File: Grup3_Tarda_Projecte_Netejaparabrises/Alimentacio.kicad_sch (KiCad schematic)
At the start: 14 parts, among them IC1 L78S05CV, J1 Screw_Terminal_01x02

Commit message: canvis reles
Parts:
- FL1, FL2, FL3, FL4: footprint BLM03HD331SZ1D:BEADC0603X33N -> Projecte:BEADC0603X33N
- IC1: footprint L78S05CV:TO-220-STANDING -> Projecte:TO-220-STANDING
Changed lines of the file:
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@@
       (effects (font (size 1.27 1.27)))
     )
-    (property "Footprint" "BLM03HD331SZ1D:BEADC0603X33N" (at 95.25 134.62 0)
+    (property "Footprint" "Projecte:BEADC0603X33N" (at 95.25 134.62 0)
       (effects (font (size 1.27 1.27)) (justify bottom) hide)
     )
@@
       (effects (font (size 1.27 1.27)))
     )
-    (property "Footprint" "BLM03HD331SZ1D:BEADC0603X33N" (at 95.25 143.51 0)
+    (property "Footprint" "Projecte:BEADC0603X33N" (at 95.25 143.51 0)
       (effects (font (size 1.27 1.27)) (justify bottom) hide)
     )
@@
       (effects (font (size 1.27 1.27)))
     )
-    (property "Footprint" "BLM03HD331SZ1D:BEADC0603X33N" (at 95.25 115.57 0)
+    (property "Footprint" "Projecte:BEADC0603X33N" (at 95.25 115.57 0)
       (effects (font (size 1.27 1.27)) (justify bottom) hide)
     )
@@
       (effects (font (size 1.27 1.27)))
     )
-    (property "Footprint" "L78S05CV:TO-220-STANDING" (at 147.574 62.992 0)
+    (property "Footprint" "Projecte:TO-220-STANDING" (at 147.574 62.992 0)
       (effects (font (size 1.27 1.27)) (justify bottom) hide)
     )
@@
       (effects (font (size 1.27 1.27)))
     )
-    (property "Footprint" "BLM03HD331SZ1D:BEADC0603X33N" (at 95.25 124.46 0)
-      (effects (font (size 1.27 1.27)) (justify bottom) hide)
-    )
+    (property "Footprint" "Projecte:BEADC0603X33N" (at 95.25 124.46 0)
+      (effects (font (size 1.27 1.27)) (justify bottom) hide)
+    )

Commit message: Layout 3
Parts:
- FL1, FL2, FL3, FL4: footprint Projecte:BEADC0603X33N -> BLM03HD331SZ1D:BEADC0603X33N
- IC1: footprint Projecte:TO-220-STANDING -> L78S05CV:TO-220-STANDING
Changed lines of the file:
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@@
   (title_block
     (title "Projecte Netejaparabrises - Grup 4 Tarda")
-    (date "2023-04-12")
-    (rev "v1.2.12042023")
+    (date "2023-04-05")
+    (rev "v1.1.05042023")
   )
   (junction (at 132.334 62.992) (diameter 0) (color 0 0 0 0)
@@
       (effects (font (size 1.27 1.27)))
     )
-    (property "Footprint" "Projecte:BEADC0603X33N" (at 95.25 134.62 0)
+    (property "Footprint" "BLM03HD331SZ1D:BEADC0603X33N" (at 95.25 134.62 0)
       (effects (font (size 1.27 1.27)) (justify bottom) hide)
     )
@@
       (effects (font (size 1.27 1.27)))
     )
-    (property "Footprint" "Projecte:BEADC0603X33N" (at 95.25 143.51 0)
+    (property "Footprint" "BLM03HD331SZ1D:BEADC0603X33N" (at 95.25 143.51 0)
       (effects (font (size 1.27 1.27)) (justify bottom) hide)
     )
@@
       (effects (font (size 1.27 1.27)))
     )
-    (property "Footprint" "Projecte:BEADC0603X33N" (at 95.25 115.57 0)
+    (property "Footprint" "BLM03HD331SZ1D:BEADC0603X33N" (at 95.25 115.57 0)
       (effects (font (size 1.27 1.27)) (justify bottom) hide)
     )
@@
       (effects (font (size 1.27 1.27)))
     )
-    (property "Footprint" "Projecte:TO-220-STANDING" (at 147.574 62.992 0)
+    (property "Footprint" "L78S05CV:TO-220-STANDING" (at 147.574 62.992 0)
       (effects (font (size 1.27 1.27)) (justify bottom) hide)
     )
@@
       (effects (font (size 1.27 1.27)))
     )
-    (property "Footprint" "Projecte:BEADC0603X33N" (at 95.25 124.46 0)
-      (effects (font (size 1.27 1.27)) (justify bottom) hide)
-    )
+    (property "Footprint" "BLM03HD331SZ1D:BEADC0603X33N" (at 95.25 124.46 0)
+      (effects (font (size 1.27 1.27)) (justify bottom) hide)
+    )

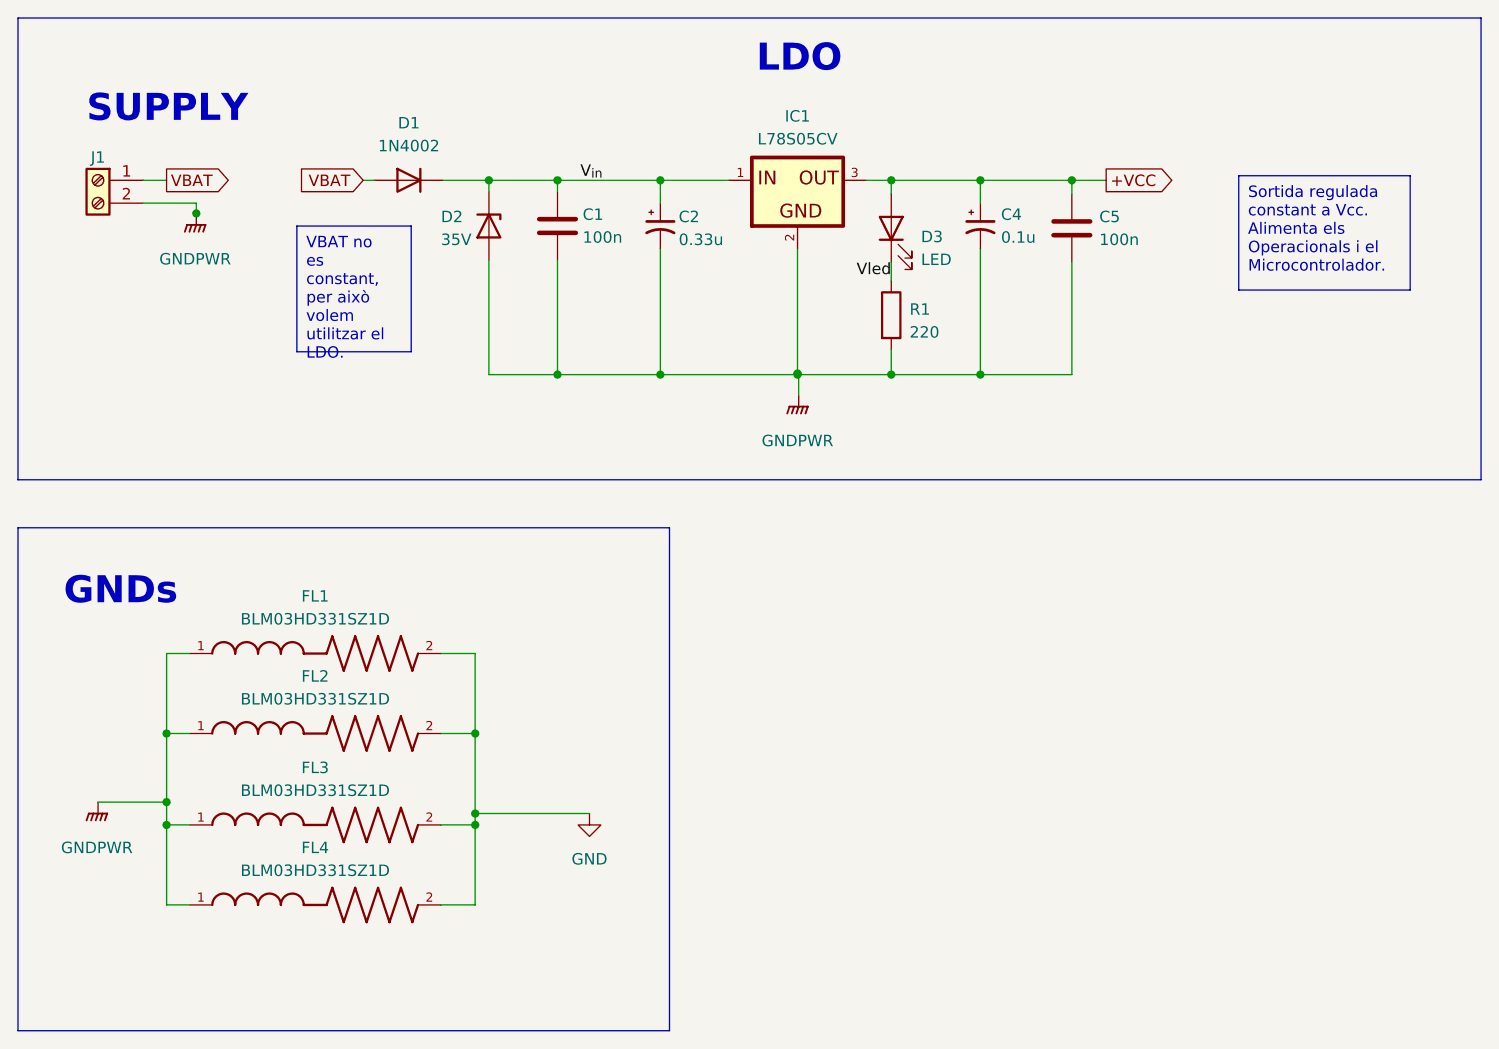
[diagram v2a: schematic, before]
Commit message: canvis divisor sensor de pluja, node vbat protegit, connector de motors, README
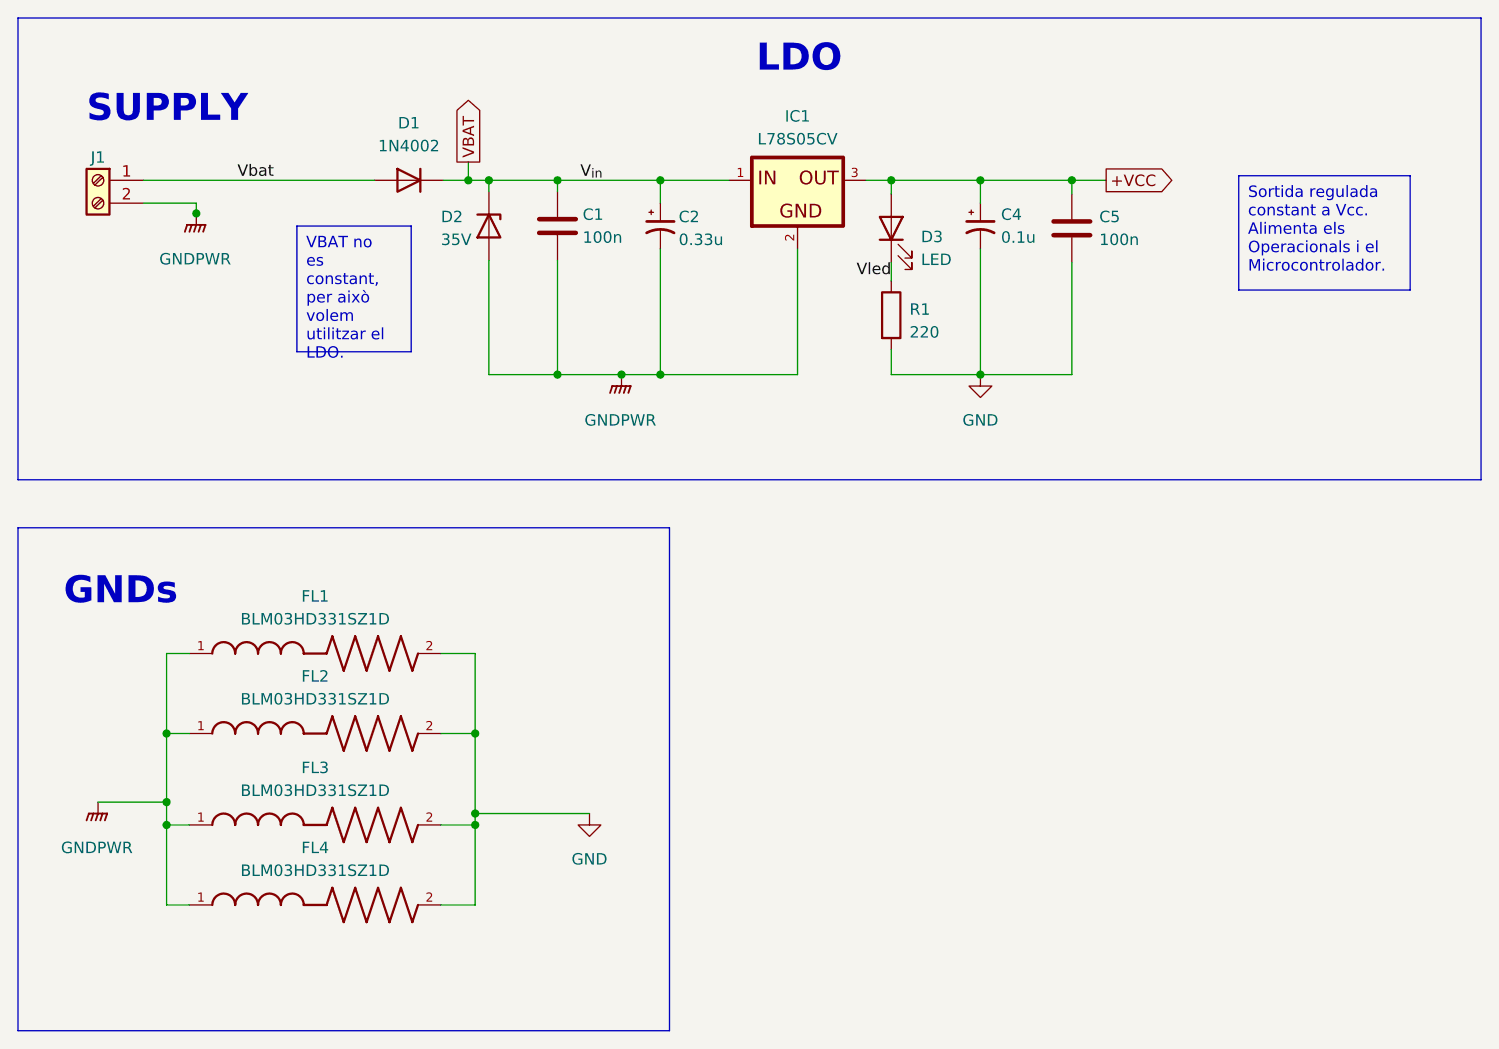
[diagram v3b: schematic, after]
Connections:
- net V_{in} is gone; now on net VBAT: C1.1, C2.1, D1.1 (K), D2.1 (K), IC1.1
- net GND: now also C4.2, C5.2, R1.2
- net GNDPWR: no longer C4.2, C5.2, R1.2
- net VBAT: no longer D1.2 (A), J1.1 (Pin_1)
- new net Vbat: D1.2 (A), J1.1 (Pin_1)

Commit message: placement
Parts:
- J1: footprint Connector_PinSocket_2.54mm:PinSocket_1x02_P2.54mm_Vertical -> TerminalBlock_Phoenix:TerminalBlock_Phoenix_MKDS-1,5-2-5.08_1x02_P5.08mm_Horizontal
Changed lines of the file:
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@@
       (effects (font (size 1.27 1.27)) hide)
     )
-    (property "Footprint" "Connector_PinSocket_2.54mm:PinSocket_1x02_P2.54mm_Vertical" (at 69.85 62.992 0)
+    (property "Footprint" "TerminalBlock_Phoenix:TerminalBlock_Phoenix_MKDS-1,5-2-5.08_1x02_P5.08mm_Horizontal" (at 69.85 62.992 0)
       (effects (font (size 1.27 1.27)) hide)
     )

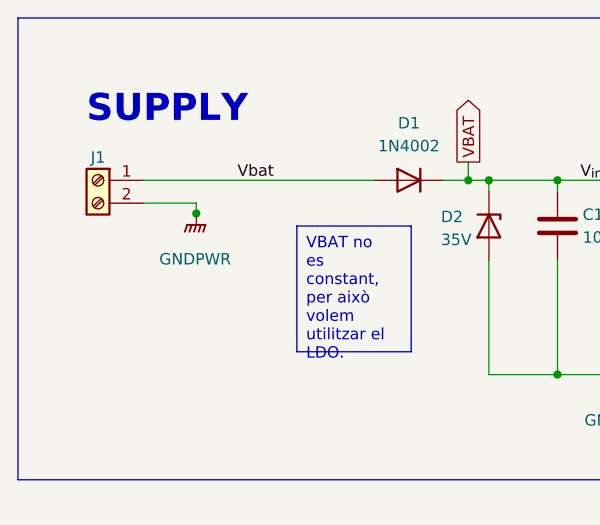
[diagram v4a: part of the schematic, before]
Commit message: plans de massa i alimentacio layout
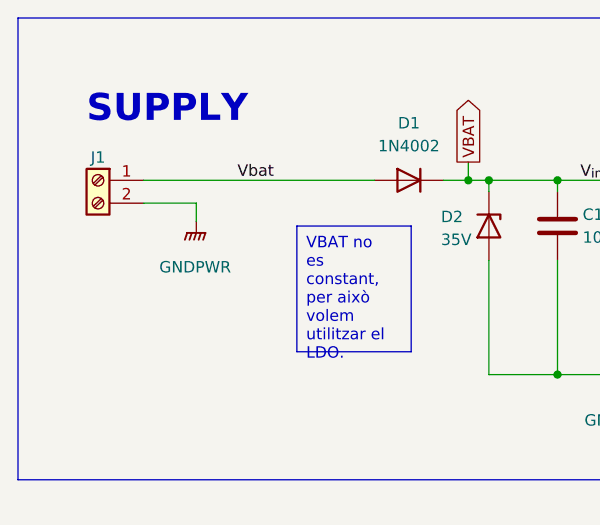
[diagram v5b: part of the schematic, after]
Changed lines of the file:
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@@
   (junction (at 167.894 84.582) (diameter 0) (color 0 0 0 0)
   )
-  (junction (at 80.772 66.675) (diameter 0) (color 0 0 0 0)
-  )
   (junction (at 77.47 134.62) (diameter 0) (color 0 0 0 0)
   )
@@
     (stroke (width 0) (type default))
   )
-  (wire (pts (xy 80.772 66.675) (xy 80.772 66.929))
-    (stroke (width 0) (type default))
-  )
   (wire (pts (xy 128.016 84.582) (xy 132.334 84.582))
     (stroke (width 0) (type default))
@@
     (stroke (width 0) (type default))
   )
-  (wire (pts (xy 80.772 65.532) (xy 80.772 66.675))
+  (wire (pts (xy 80.772 65.532) (xy 80.772 67.564))
     (stroke (width 0) (type default))
   )
@@
     )
   )
-  (symbol (lib_id "power:GNDPWR") (at 80.772 66.675 0) (unit 1)
-    (in_bom yes) (on_board yes) (dnp no) (fields_autoplaced)
-    (property "Reference" "#PWR02" (at 80.772 71.755 0)
-      (effects (font (size 1.27 1.27)) hide)
-    )
-    (property "Value" "GNDPWR" (at 80.645 71.755 0)
-      (effects (font (size 1.27 1.27)))
-    )
-    (property "Footprint" "" (at 80.772 67.945 0)
-      (effects (font (size 1.27 1.27)) hide)
-    )
-    (property "Datasheet" "" (at 80.772 67.945 0)
-      (effects (font (size 1.27 1.27)) hide)
-    )
+  (symbol (lib_id "power:GNDPWR") (at 80.772 67.564 0) (unit 1)
+    (in_bom yes) (on_board yes) (dnp no) (fields_autoplaced)
+    (property "Reference" "#PWR02" (at 80.772 72.644 0)
+      (effects (font (size 1.27 1.27)) hide)
+    )
+    (property "Value" "GNDPWR" (at 80.645 72.644 0)
+      (effects (font (size 1.27 1.27)))
+    )
+    (property "Footprint" "" (at 80.772 68.834 0)
+      (effects (font (size 1.27 1.27)) hide)
+    )
+    (property "Datasheet" "" (at 80.772 68.834 0)
+      (effects (font (size 1.27 1.27)) hide)
+    )

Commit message: routing v1 sense acabar
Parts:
- removed D2: 35V, Diode_THT:D_5W_P5.08mm_Vertical_AnodeUp, symbol Device:D_Zener
- C1, C5: footprint Capacitor_SMD:C_0805_2012Metric -> Capacitor_THT:C_Disc_D3.0mm_W1.6mm_P2.50mm
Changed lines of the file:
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@@
   (junction (at 132.334 62.992) (diameter 0) (color 0 0 0 0)
   )
-  (junction (at 113.284 62.992) (diameter 0) (color 0 0 0 0)
-  )
-  (junction (at 120.904 84.582) (diameter 0) (color 0 0 0 0)
-  )
   (junction (at 132.334 84.582) (diameter 0) (color 0 0 0 0)
   )
@@
   (junction (at 128.016 84.582) (diameter 0) (color 0 0 0 0)
   )
-  (junction (at 110.998 62.992) (diameter 0) (color 0 0 0 0)
-  )
   (junction (at 77.47 132.08) (diameter 0) (color 0 0 0 0)
   )
@@
   (junction (at 77.47 124.46) (diameter 0) (color 0 0 0 0)
   )
+  (junction (at 114.554 62.992) (diameter 0) (color 0 0 0 0)
+  )
   (wire (pts (xy 120.904 84.582) (xy 128.016 84.582))
     (stroke (width 0) (type default))
@@
     (stroke (width 0) (type default))
   )
-  (wire (pts (xy 113.284 71.882) (xy 113.284 84.582))
+  (wire (pts (xy 114.554 62.992) (xy 120.904 62.992))
     (stroke (width 0) (type default))
   )
@@
     (stroke (width 0) (type default))
   )
-  (wire (pts (xy 113.284 62.992) (xy 120.904 62.992))
-    (stroke (width 0) (type default))
-  )
   (wire (pts (xy 120.904 62.992) (xy 132.334 62.992))
     (stroke (width 0) (type default))
@@
     (stroke (width 0) (type default))
   )
-  (wire (pts (xy 113.284 84.582) (xy 120.904 84.582))
-    (stroke (width 0) (type default))
-  )
   (wire (pts (xy 167.894 62.992) (xy 178.054 62.992))
     (stroke (width 0) (type default))
@@
     (stroke (width 0) (type default))
   )
-  (wire (pts (xy 108.204 62.992) (xy 110.998 62.992))
+  (wire (pts (xy 108.204 62.992) (xy 114.554 62.992))
     (stroke (width 0) (type default))
   )
@@
     (stroke (width 0) (type default))
   )
-  (wire (pts (xy 113.284 62.992) (xy 113.284 64.262))
-    (stroke (width 0) (type default))
-  )
-  (wire (pts (xy 110.998 60.96) (xy 110.998 62.992))
+  (wire (pts (xy 114.554 60.96) (xy 114.554 62.992))
     (stroke (width 0) (type default))
   )
@@
   )
   (wire (pts (xy 111.76 134.62) (xy 111.76 133.35))
-    (stroke (width 0) (type default))
-  )
-  (wire (pts (xy 110.998 62.992) (xy 113.284 62.992))
     (stroke (width 0) (type default))
   )
@@
     )
   )
-  (global_label "VBAT" (shape output) (at 110.998 60.96 90) (fields_autoplaced)
+  (global_label "VBAT" (shape output) (at 114.554 60.96 90) (fields_autoplaced)
     (effects (font (size 1.27 1.27)) (justify left))
-    (property "Intersheetrefs" "${INTERSHEET_REFS}" (at 110.998 53.6394 90)
+    (property "Intersheetrefs" "${INTERSHEET_REFS}" (at 114.554 53.6394 90)
       (effects (font (size 1.27 1.27)) (justify left) hide)
     )
@@
       (effects (font (size 1.27 1.27)) (justify left))
     )
-    (property "Footprint" "Capacitor_SMD:C_0805_2012Metric" (at 121.8692 71.882 0)
+    (property "Footprint" "Capacitor_THT:C_Disc_D3.0mm_W1.6mm_P2.50mm" (at 121.8692 71.882 0)
       (effects (font (size 1.27 1.27)) hide)
     )
@@
       (effects (font (size 1.27 1.27)) (justify left))
     )
-    (property "Footprint" "Capacitor_SMD:C_0805_2012Metric" (at 179.0192 72.136 0)
+    (property "Footprint" "Capacitor_THT:C_Disc_D3.0mm_W1.6mm_P2.50mm" (at 179.0192 72.136 0)
       (effects (font (size 1.27 1.27)) hide)
     )
@@
         )
       )
-    )
-  )
-  (symbol (lib_id "Device:D_Zener") (at 113.284 68.072 270) (unit 1)
-    (in_bom yes) (on_board yes) (dnp no)
-    (property "Reference" "D2" (at 107.95 67.0559 90)
-      (effects (font (size 1.27 1.27)) (justify left))
-    )
-    (property "Value" "35V" (at 107.95 69.596 90)
-      (effects (font (size 1.27 1.27)) (justify left))
-    )
-    (property "Footprint" "Diode_THT:D_5W_P5.08mm_Vertical_AnodeUp" (at 113.284 68.072 0)
-      (effects (font (size 1.27 1.27)) hide)
-    )
-    (property "Datasheet" "~" (at 113.284 68.072 0)
-      (effects (font (size 1.27 1.27)) hide)
-    )
-    (pin "1")
-    (pin "2")
-    (instances
-      (project ""
-        (path "/471896f9-a17e-46cb-bb6a-e6efc81f054f"
-          (reference "D2") (unit 1)
-        )
-      )
-      (project "Grup3_Tarda_Projecte_Netejaparabrises"
-        (path "/7ae78f34-680b-4fd9-8391-ce3e1c73c4b5"
-          (reference "D2") (unit 1)
-        )
-        (path "/7ae78f34-680b-4fd9-8391-ce3e1c73c4b5/de573664-441d-44bf-8893-2d2e822d4a99"
-          (reference "D2") (unit 1)
-        )
-      )
-      (project "AidarIglesias_DavidMiravent_P3"
-        (path "/f9f603a9-b774-48a7-94d1-4c8d3d65a3f8"
-          (reference "D2") (unit 1)
-        )
-      )

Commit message: placing rooting
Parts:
- C1, C2, C4, C5: footprint Capacitor_THT:C_Disc_D3.0mm_W1.6mm_P2.50mm -> Capacitor_SMD:C_0805_2012Metric_Pad1.18x1.45mm_HandSolder
- IC1: footprint L78S05CV:TO-220-STANDING -> Libreia:TO-220-3_Horizontal_TabDown_mod
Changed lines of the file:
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@@
       (effects (font (size 1.27 1.27)) (justify left))
     )
-    (property "Footprint" "Capacitor_THT:C_Disc_D3.0mm_W1.6mm_P2.50mm" (at 167.894 68.072 0)
+    (property "Footprint" "Capacitor_SMD:C_0805_2012Metric_Pad1.18x1.45mm_HandSolder" (at 167.894 68.072 0)
       (effects (font (size 1.27 1.27)) hide)
     )
@@
       (effects (font (size 1.27 1.27)))
     )
-    (property "Footprint" "L78S05CV:TO-220-STANDING" (at 147.574 62.992 0)
+    (property "Footprint" "Libreia:TO-220-3_Horizontal_TabDown_mod" (at 147.574 62.992 0)
       (effects (font (size 1.27 1.27)) (justify bottom) hide)
     )
@@
       (effects (font (size 1.27 1.27)) (justify left))
     )
-    (property "Footprint" "Capacitor_THT:C_Disc_D3.0mm_W1.6mm_P2.50mm" (at 121.8692 71.882 0)
+    (property "Footprint" "Capacitor_SMD:C_0805_2012Metric_Pad1.18x1.45mm_HandSolder" (at 121.8692 71.882 0)
       (effects (font (size 1.27 1.27)) hide)
     )
@@
       (effects (font (size 1.27 1.27)) (justify left))
     )
-    (property "Footprint" "Capacitor_THT:C_Disc_D3.0mm_W1.6mm_P2.50mm" (at 132.334 68.072 0)
+    (property "Footprint" "Capacitor_SMD:C_0805_2012Metric_Pad1.18x1.45mm_HandSolder" (at 132.334 68.072 0)
       (effects (font (size 1.27 1.27)) hide)
     )
@@
       (effects (font (size 1.27 1.27)) (justify left))
     )
-    (property "Footprint" "Capacitor_THT:C_Disc_D3.0mm_W1.6mm_P2.50mm" (at 179.0192 72.136 0)
-      (effects (font (size 1.27 1.27)) hide)
-    )
+    (property "Footprint" "Capacitor_SMD:C_0805_2012Metric_Pad1.18x1.45mm_HandSolder" (at 179.0192 72.136 0)
+      (effects (font (size 1.27 1.27)) hide)
+    )
